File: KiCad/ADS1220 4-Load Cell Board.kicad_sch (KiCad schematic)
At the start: 0 parts

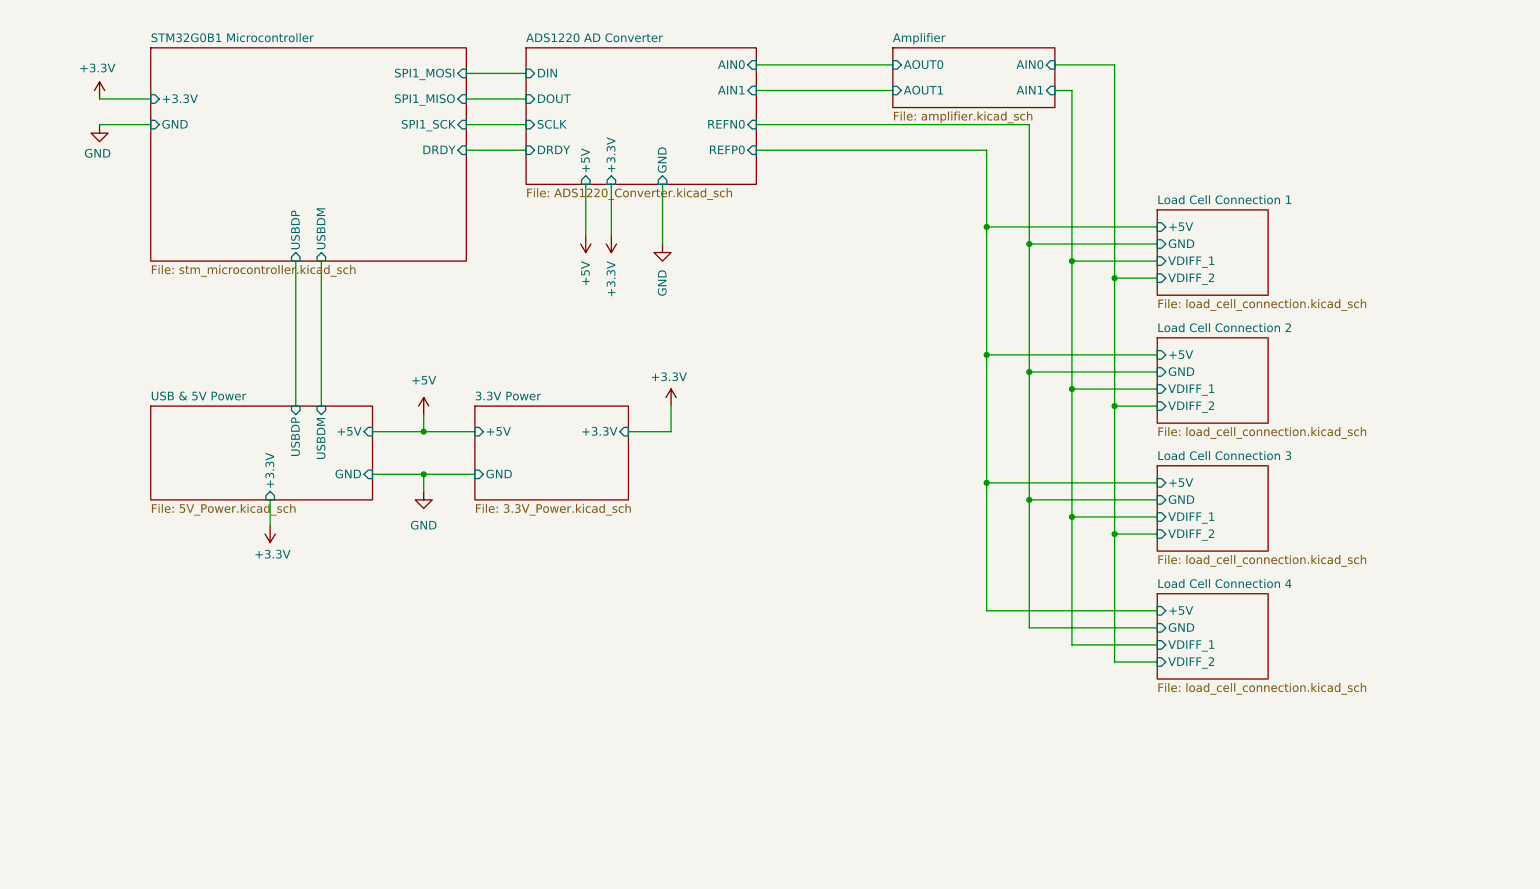
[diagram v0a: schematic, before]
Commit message: Add MCP6V92 Amplifier
Add amplifier part to amplifier block
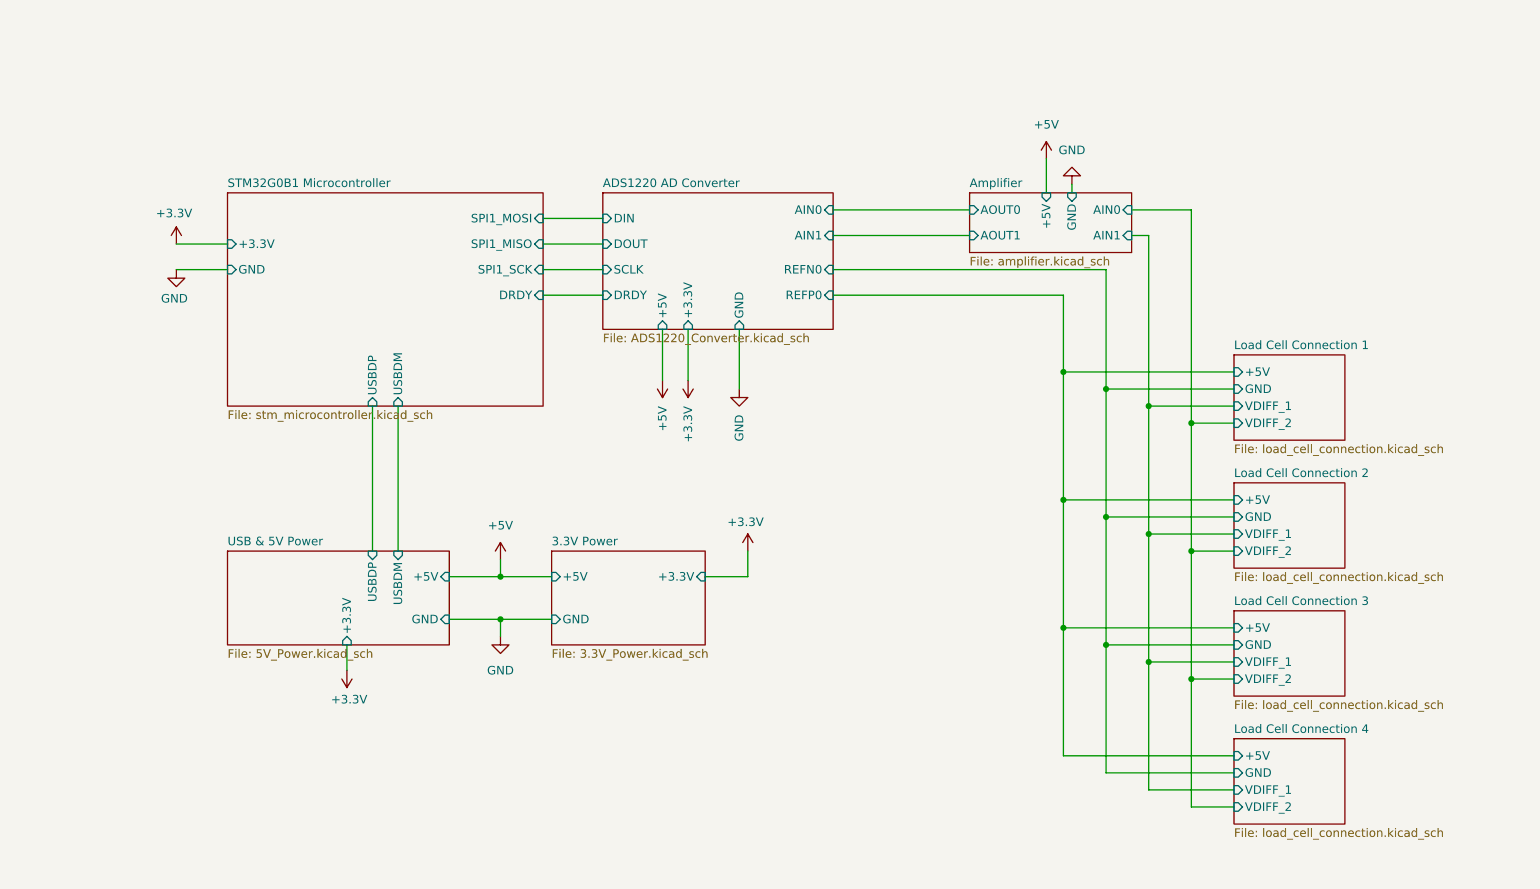
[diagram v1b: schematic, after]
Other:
- sheet Amplifier ports: added +5V, GND; removed none

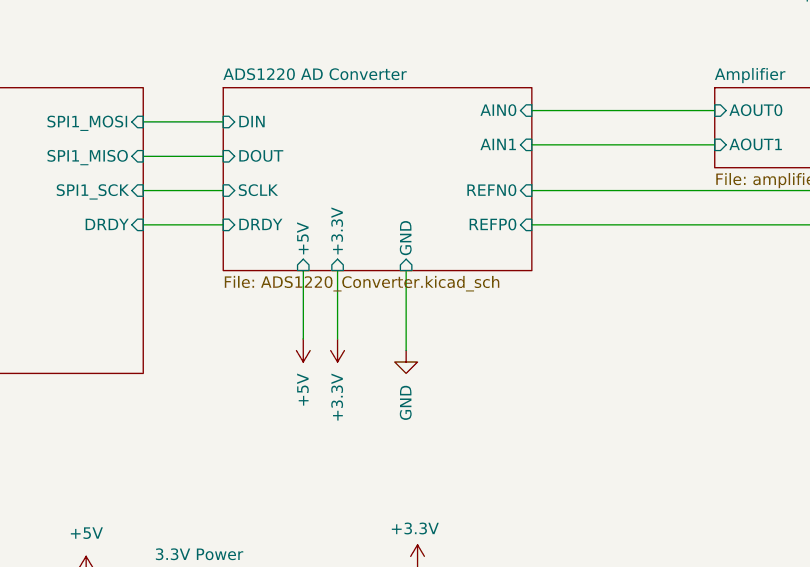
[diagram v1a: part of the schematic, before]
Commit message: Add bypass resistors for Amplifier
Add 0R resistor pads to allow the amplifier to be bypassed so we can test with/without it in the circuit.
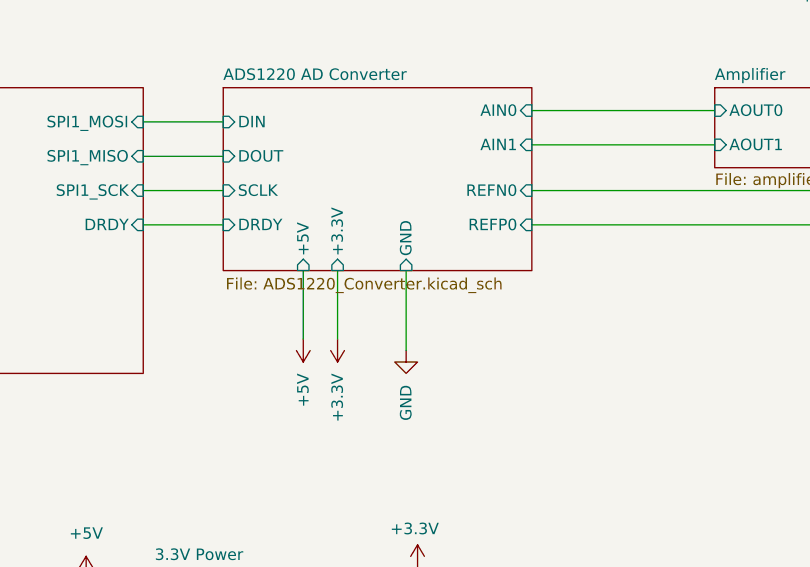
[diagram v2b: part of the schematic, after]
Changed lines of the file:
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@@
 		(at 119.38 48.26)
 		(size 34.29 20.32)
-		(fields_autoplaced yes)
 		(stroke
 			(width 0.1524)
@@
 		)
 		(property "Sheetfile" "ADS1220_Converter.kicad_sch"
-			(at 119.38 69.1646 0)
+			(at 119.634 69.342 0)
 			(effects
 				(font

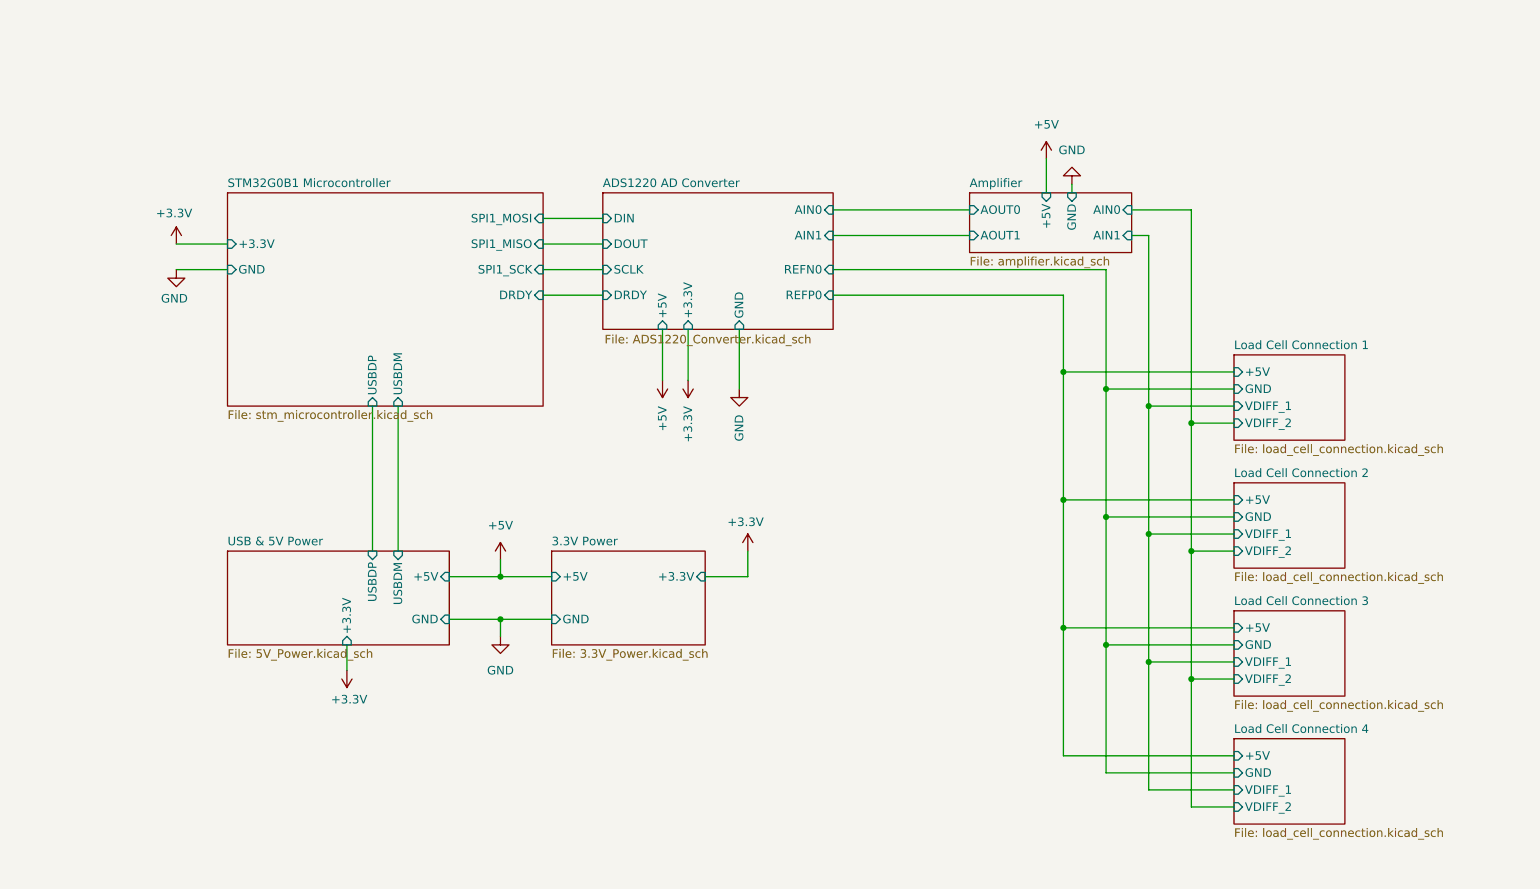
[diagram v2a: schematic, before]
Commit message: Use 12V Power
* Use 12 V Power
* Update to an F103 processor with better compatibility with Katapult
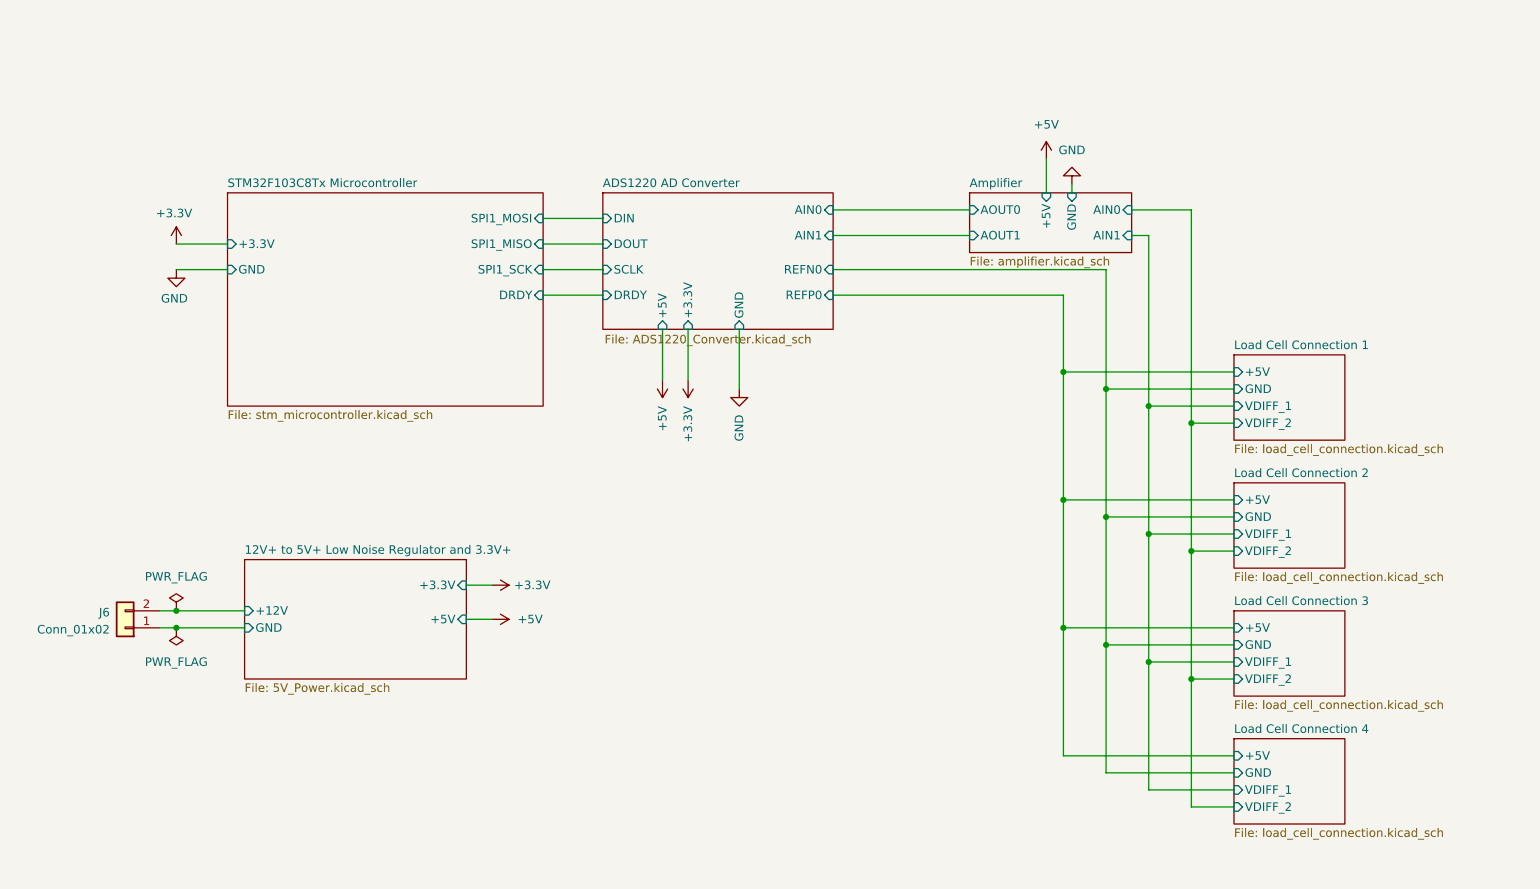
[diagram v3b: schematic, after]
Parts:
- added J6: Conn_01x02, Connector_JST:JST_XH_S2B-XH-A-1_1x02_P2.50mm_Horizontal, symbol Connector_Generic:Conn_01x02
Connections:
- new net 12V+ to 5V+ Low Noise Regulator and 3.3V+/+12V: J6.2 (Pin_2)
- new net 12V+ to 5V+ Low Noise Regulator and 3.3V+/GND: J6.1 (Pin_1)
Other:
- sheet STM32G0B1 Microcontroller renamed STM32F103C8Tx Microcontroller
- sheet USB & 5V Power renamed 12V+ to 5V+ Low Noise Regulator and 3.3V+
- removed sheet 3.3V Power
- sheet 12V+ to 5V+ Low Noise Regulator and 3.3V+ ports: added +12V; removed USBDM, USBDP
- sheet STM32F103C8Tx Microcontroller ports: added none; removed USBDM, USBDP

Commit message: Initial Routing
Taking a first pass at layout of the PCB
* load cell connectors were moved to the root schematic and placed on a bus to facilitate PCB routing
* Nets for the filters were directly connected to remove the confusion about GND verses REFN
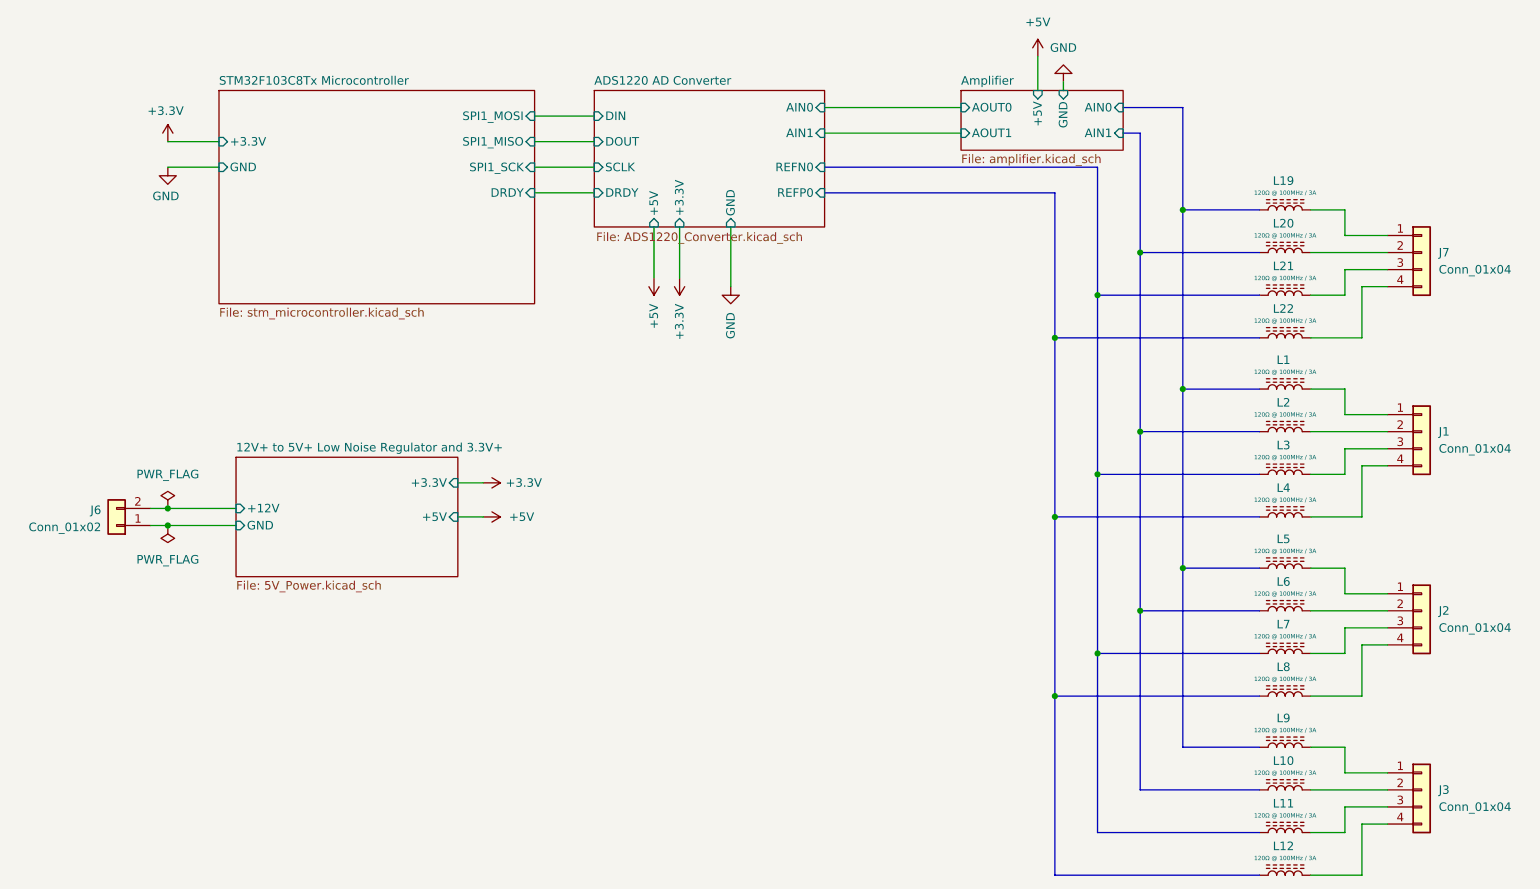
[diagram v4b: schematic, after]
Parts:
- added J1, J2, J3, J7: Conn_01x04, Connector_JST:JST_XH_S4B-XH-A-1_1x04_P2.50mm_Horizontal, symbol Connector_Generic:Conn_01x04
- added L1, L10, L11, L12, L19, L2, L20, L21, L22, L3, L4, L5, L6, L7, L8, L9: 120Ω @ 100MHz / 3A, Inductor_SMD:L_0805_2012Metric_Pad1.05x1.20mm_HandSolder, symbol Device:L_Ferrite
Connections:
- new net: J7.2 (Pin_2), L20.2
- new net: J1.2 (Pin_2), L2.2
- new net: J7.1 (Pin_1), L19.2
- new net: J7.3 (Pin_3), L21.2
- new net: J7.4 (Pin_4), L22.2
- new net: J3.4 (Pin_4), L12.2
- new net: J1.3 (Pin_3), L3.2
- new net: J1.4 (Pin_4), L4.2
- new net: J1.1 (Pin_1), L1.2
- new net: J3.1 (Pin_1), L9.2
- new net: J3.2 (Pin_2), L10.2
- new net: J3.3 (Pin_3), L11.2
- new net: J2.1 (Pin_1), L5.2
- new net: J2.2 (Pin_2), L6.2
- new net: J2.4 (Pin_4), L8.2
- new net: J2.3 (Pin_3), L7.2
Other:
- removed sheet Load Cell Connection 1
- removed sheet Load Cell Connection 2
- removed sheet Load Cell Connection 3
- removed sheet Load Cell Connection 4
- moved on the sheet: J6

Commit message: Convert Power to LDOs
Convert power section to use only LDOs. This means we will only get 4.75V or 4.5V on the analog line but this comes with greatly increased simplicity of layout.
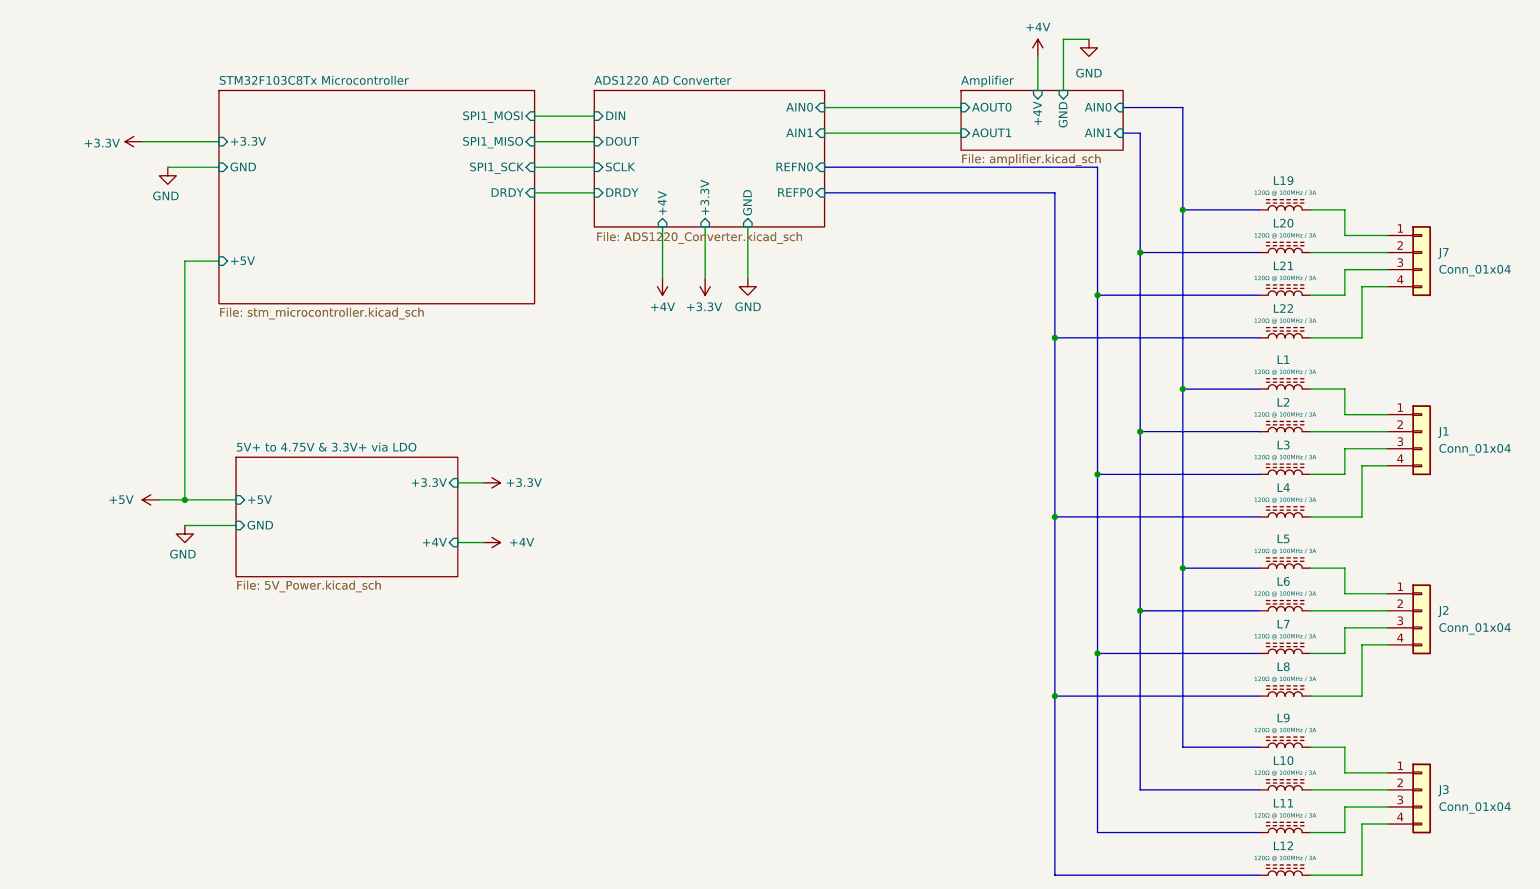
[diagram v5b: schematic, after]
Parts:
- removed J6: Conn_01x02, Connector_JST:JST_XH_S2B-XH-A-1_1x02_P2.50mm_Horizontal, symbol Connector_Generic:Conn_01x02
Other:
- sheet 12V+ to 5V+ Low Noise Regulator and 3.3V+ renamed 5V+ to 4.75V & 3.3V+ via LDO
- sheet 5V+ to 4.75V & 3.3V+ via LDO ports: added +4V; removed +12V
- sheet ADS1220 AD Converter ports: added +4V; removed +5V
- sheet Amplifier ports: added +4V; removed +5V
- sheet STM32F103C8Tx Microcontroller ports: added +5V; removed none
